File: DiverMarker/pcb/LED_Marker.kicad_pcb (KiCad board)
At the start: 2 copper layers, 75 x 20 mm, 26 parts, among them IC101 PIC16LF15313, J101 SKEDD6, Q100 BST-52, Q101 BST-52, SW101 MK15-C2

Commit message: Working on PCB documentation
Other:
- board text added: "R1.1"
- board text removed: "R1.0"
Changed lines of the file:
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@@
 		(allow_soldermask_bridges_in_footprints no)
 		(tenting front back)
+		(grid_origin 100 120)
 		(pcbplotparams
 			(layerselection 0x00000000_00000000_55555555_5755f5ff)
@@
 		(tags "resistor handsolder")
 		(property "Reference" "R109"
-			(at 0 -1.65 0)
+			(at -0.227064 1.625 0)
 			(layer "F.SilkS")
 			(effects
@@
 		(tags "resistor handsolder")
 		(property "Reference" "R108"
-			(at 0 -1.65 0)
+			(at -0.195 1.62 0)
 			(layer "F.SilkS")
 			(effects
@@
 		(layer "User.1")
 	)
-	(gr_text "R1.0"
+	(gr_text "R1.1"
 		(at 100.9 103.3 0)
 		(layer "F.Cu")
@@
 	)
 	(gr_text "Diver marker"
+		(at 142.6 109.5 0)
+		(layer "F.Cu")
+		(effects
+			(font
+				(size 1.8 1.8)
+				(thickness 0.4)
+				(bold yes)
+			)
+			(justify left bottom)
+		)
+	)
+	(gr_text "Diver marker"
 		(at 174.3 101.2 90)
 		(layer "B.Cu")
@@
 	)
 	(segment
-		(start 140.785 110.965)
-		(end 141.75 110)
-		(width 0.8)
-		(layer "F.Cu")
-		(net 5)
-	)
-	(segment
 		(start 162 112.2)
 		(end 162 110)
@@
 	)
 	(segment
-		(start 141.75 110)
-		(end 162 110)
+		(start 139.065 110.965)
+		(end 136.465 110.965)
 		(width 0.8)
 		(layer "F.Cu")
@@
 	)
 	(segment
-		(start 139.065 110.965)
-		(end 140.785 110.965)
+		(start 160.4 110)
+		(end 162 110)
 		(width 0.8)
 		(layer "F.Cu")
@@
 	)
 	(segment
-		(start 139.065 110.965)
-		(end 136.465 110.965)
+		(start 159.435 110.965)
+		(end 160.4 110)
 		(width 0.8)
 		(layer "F.Cu")
@@
 		(width 0.8)
 		(layer "F.Cu")
+		(net 5)
+	)
+	(segment
+		(start 139.065 110.965)
+		(end 159.435 110.965)
+		(width 0.8)
+		(layer "F.Cu")

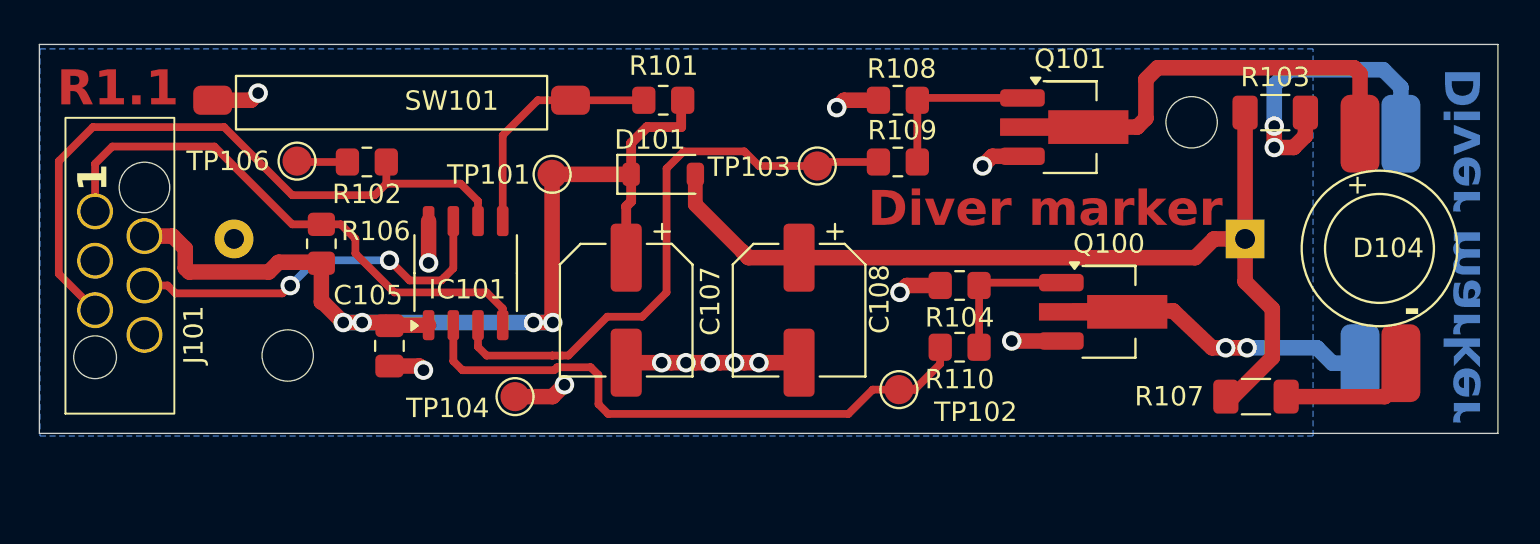
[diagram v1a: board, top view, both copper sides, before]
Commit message: Component placement optimisation. No functional changes
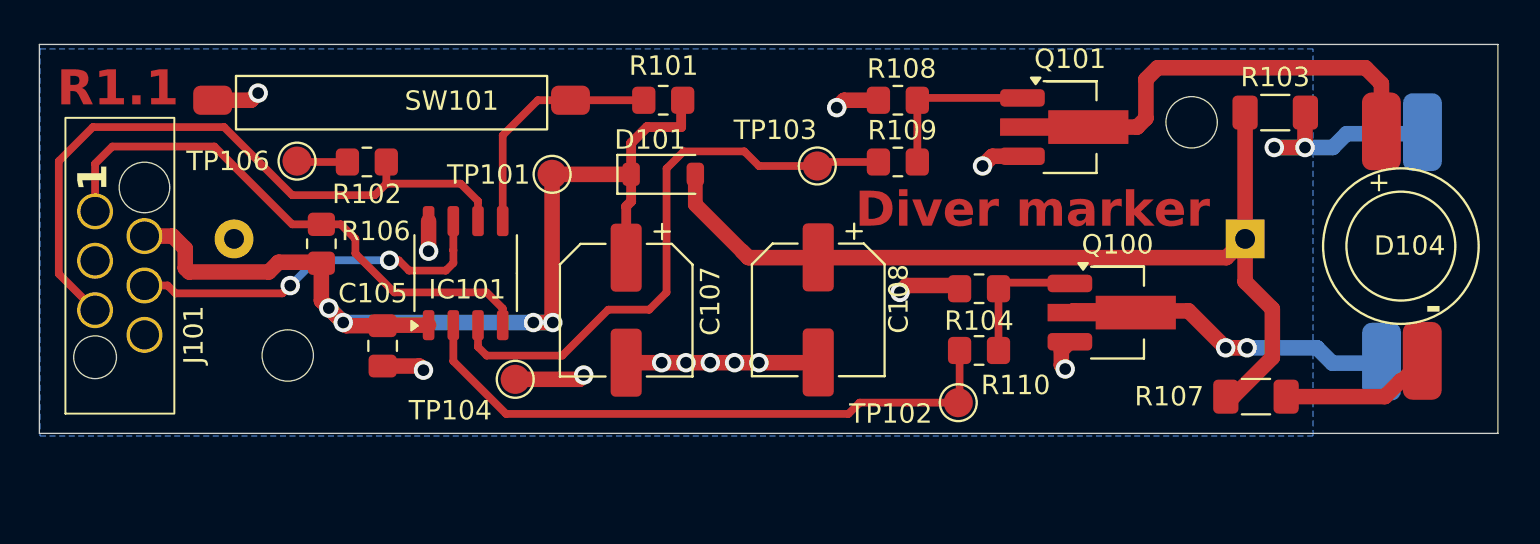
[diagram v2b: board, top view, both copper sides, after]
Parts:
- moved TP102 3.12 mm to (147.2, 118.4)
- moved D103 1.11 mm to (170.0, 110.4)
- moved D104 1.11 mm to (170.0, 110.4)
- moved R104 1.01 mm to (148.3, 112.6)
- moved R110 1.01 mm to (148.3, 115.7)
- moved C108 0.99 mm to (140.1, 113.7)
- moved TP104 0.89 mm to (124.5, 117.2)
- moved Q100 0.44 mm to (155.4, 113.8)
- moved C105 0.35 mm to (117.7, 115.5)
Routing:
- net /A_D103: track 16.9 -> 11.3 mm
- net GND: track 27.5 -> 29.2 mm
- net BlueOn: track 30.9 -> 32.0 mm
- net /PWR_MCU: track 52.4 -> 53.4 mm
- net /K_D013: track 17.5 -> 18.2 mm
- net /K_D104: track 22.9 -> 23.6 mm
- net /A_D104: track 7.14 -> 7.76 mm
- net /ICSPDAT: track 20.0 -> 19.4 mm
